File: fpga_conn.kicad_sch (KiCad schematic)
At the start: 1 part, among them J1 61082-061400LF

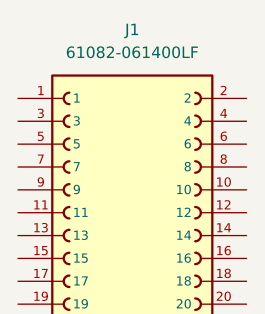
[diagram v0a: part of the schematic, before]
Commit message: Add DCCT ADCs
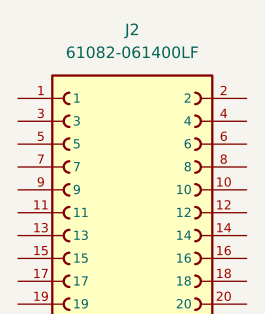
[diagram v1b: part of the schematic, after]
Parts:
- renumbered J1 to J2
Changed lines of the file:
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@@
 		(dnp no)
 		(fields_autoplaced yes)
-		(property "Reference" "J1"
+		(property "Reference" "J2"
 			(at 140.97 55.88 0)
 			(effects
@@
 			(project ""
 				(path "/40891cc8-bf64-41f4-8f69-a607d7b280eb/2218990c-df93-405e-a560-4b3f2a81eb40"
-					(reference "J1")
+					(reference "J2")
 					(unit 1)
 				)

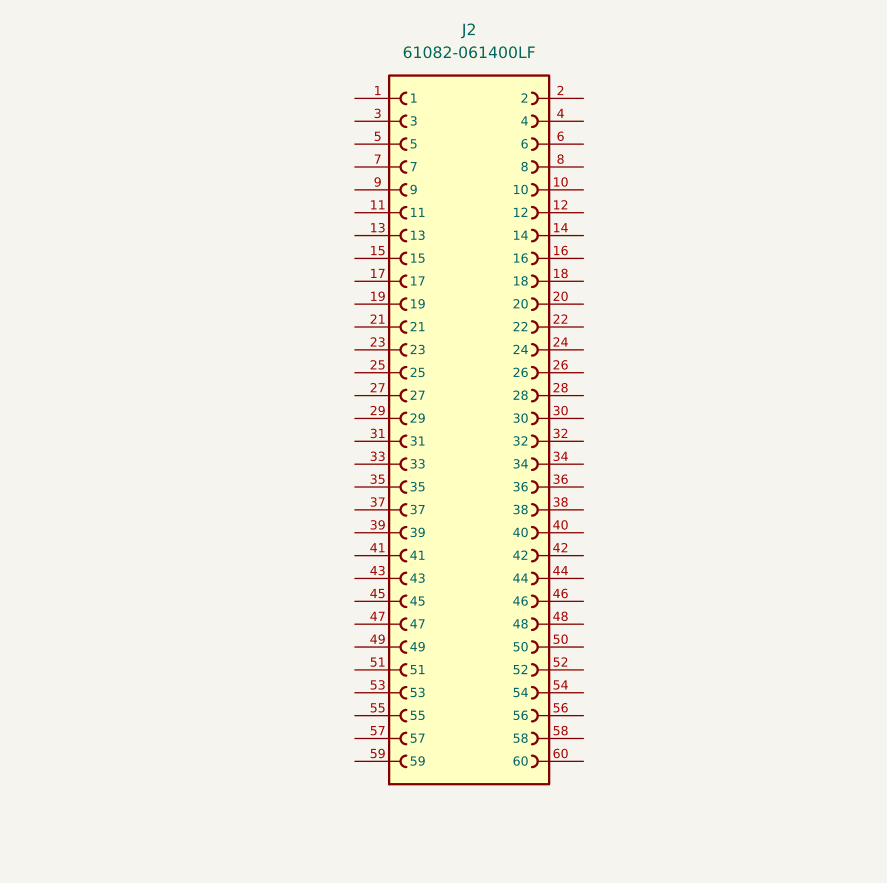
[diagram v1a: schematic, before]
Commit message: DAC and DCCT placement
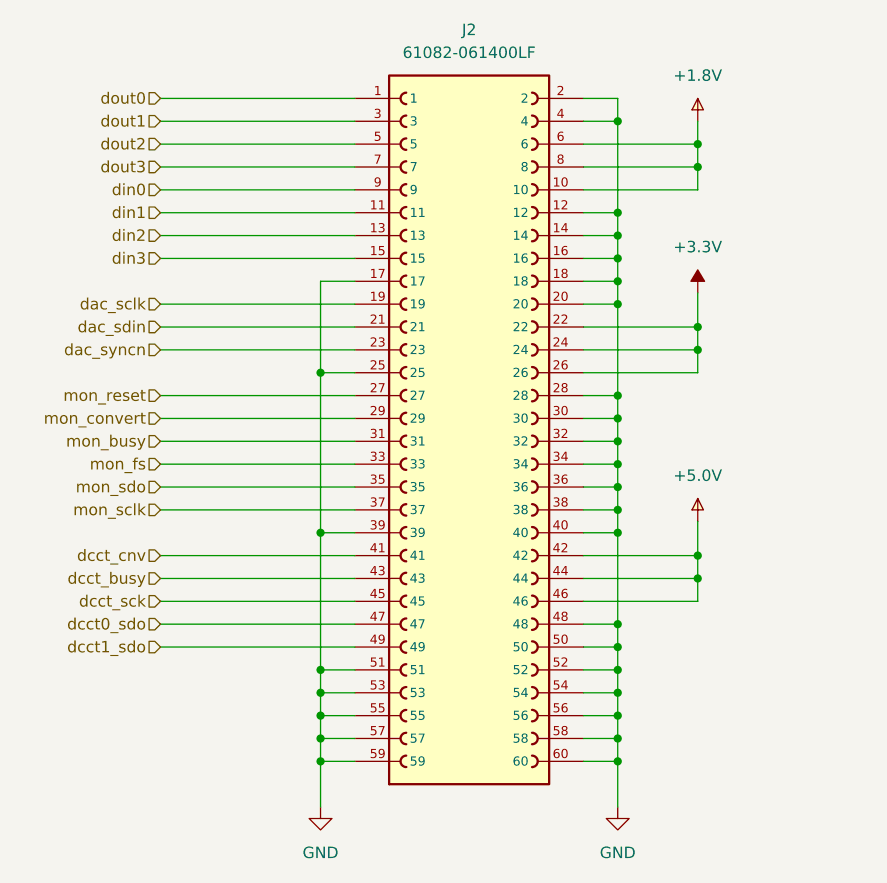
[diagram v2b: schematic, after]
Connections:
- net dout0: now reaches J2.1
- net +1.8V: now reaches J2.10
- net +1.8V: now also J2.6, J2.8
- net din1: now reaches J2.11
- net GND: now reaches J2.12
- net GND: now also J2.14, J2.16, J2.17, J2.18, J2.2, J2.20, J2.25, J2.28, J2.30, J2.32, J2.34, J2.36, J2.38, J2.39, J2.4, J2.40, J2.48, J2.50, J2.51, J2.52, J2.53, J2.54, J2.55, J2.56, J2.57, J2.58, J2.59, J2.60
- net din2: now reaches J2.13
- net din3: now reaches J2.15
- net dac_sclk: now reaches J2.19
- net dac_sdin: now reaches J2.21
- net +3.3V: now reaches J2.22
- net +3.3V: now also J2.24, J2.26
- net dac_syncn: now reaches J2.23
- net mon_reset: now reaches J2.27
- net mon_convert: now reaches J2.29
- net dout1: now reaches J2.3
- net mon_busy: now reaches J2.31
- net mon_fs: now reaches J2.33
- net mon_sdo: now reaches J2.35
- net mon_sclk: now reaches J2.37
- net dcct_cnv: now reaches J2.41
- net +5.0V: now reaches J2.42
- net +5.0V: now also J2.44, J2.46
- net dcct_busy: now reaches J2.43
- net dcct_sck: now reaches J2.45
- net dcct0_sdo: now reaches J2.47
- net dcct1_sdo: now reaches J2.49
- net dout2: now reaches J2.5
- net dout3: now reaches J2.7
- net din0: now reaches J2.9

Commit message: Tweaks to connector pinouts
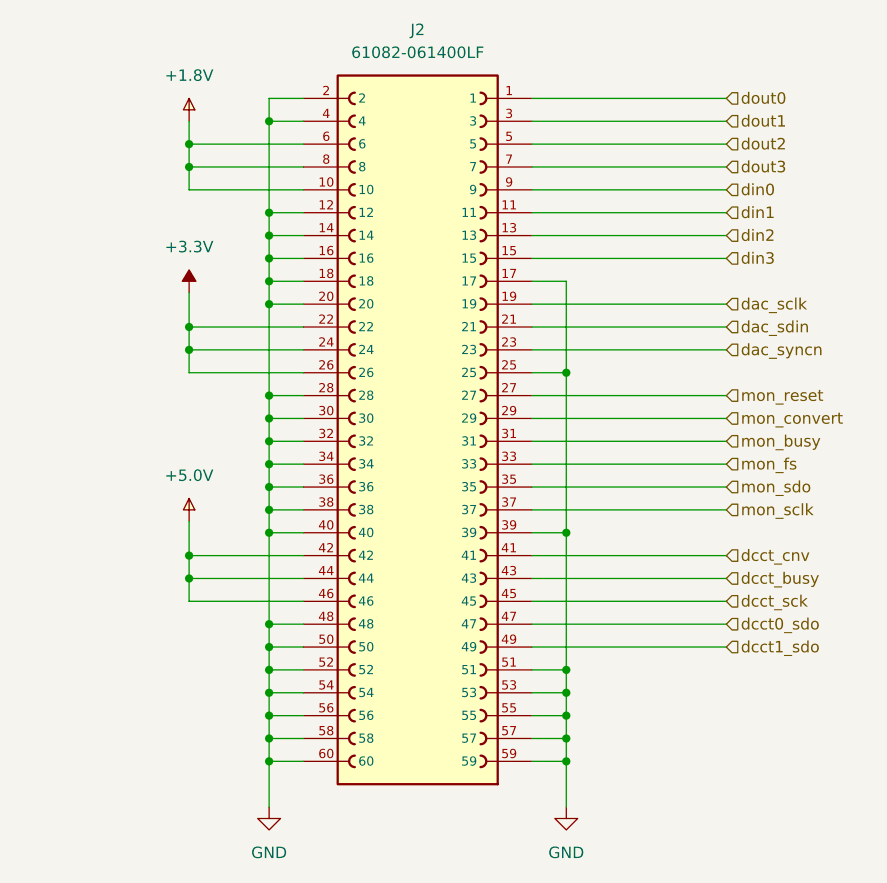
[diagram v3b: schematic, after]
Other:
- moved on the sheet: J2

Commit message: Finish layout
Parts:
- J2: Cost (none) -> 2.53; MANUFACTURER Amphenol -> (none); MFG (none) -> Amphenol; MFG_PN (none) -> 61082-061400LF
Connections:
- net GND: no longer J2.56, J2.58, J2.60
- new net +2.5V: J2.56, J2.58, J2.60
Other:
- moved on the sheet: J2
